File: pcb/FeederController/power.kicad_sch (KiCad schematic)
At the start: 20 parts, among them J17 12-24v DC, J18 5V Supply, Q1 DMP3028LK3-13, U4 AP2114-3.3, U5 AP63205WU

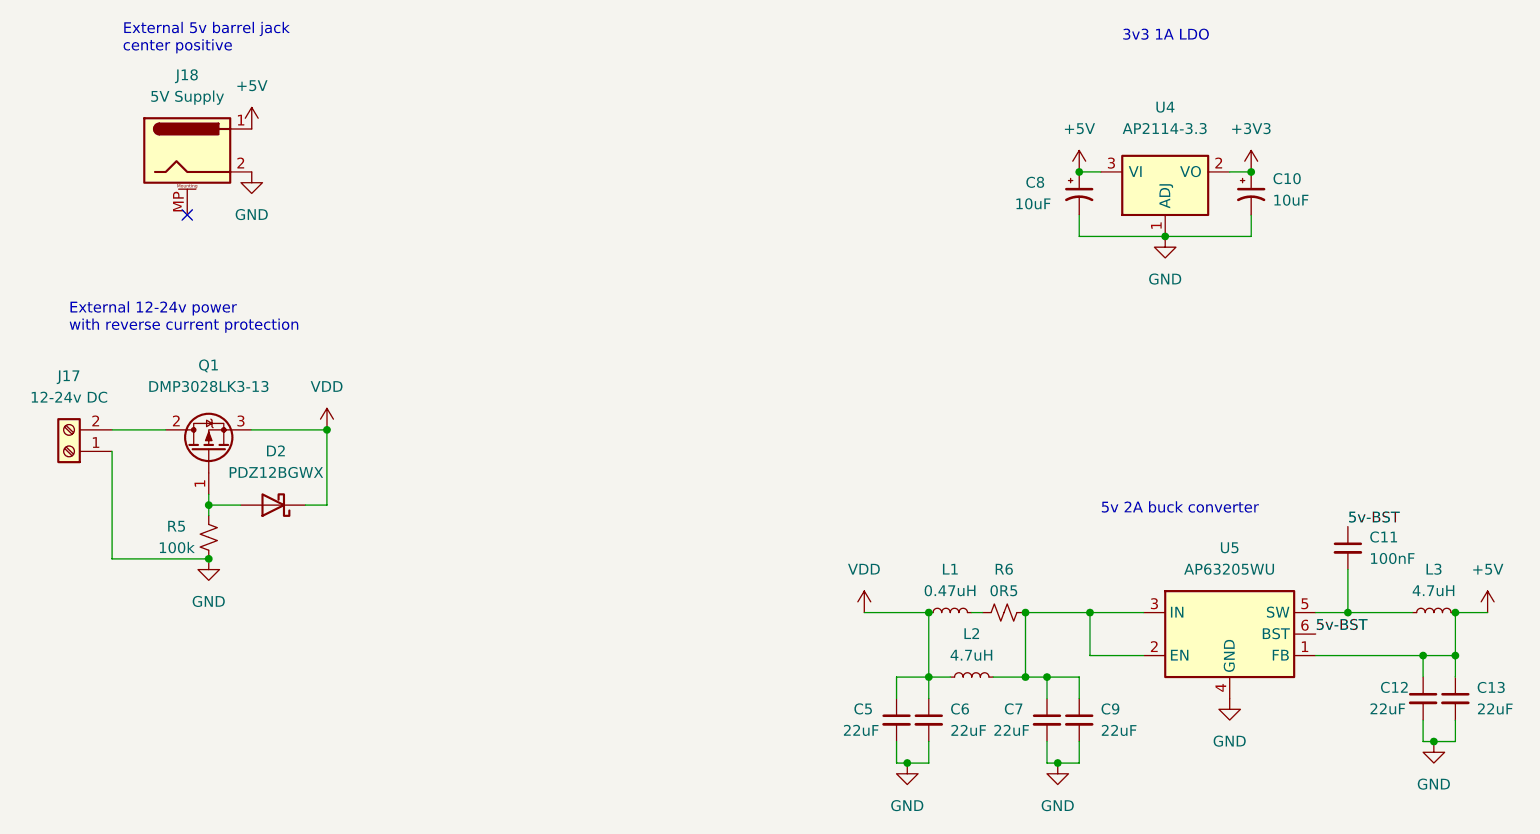
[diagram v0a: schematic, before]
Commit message: Update PCB as below
* Adjusted placement of mounting holes to line up with LumenPnP staging plate.
* Added 2k4 P/U for SDA/SCL.
* GND plane stitching
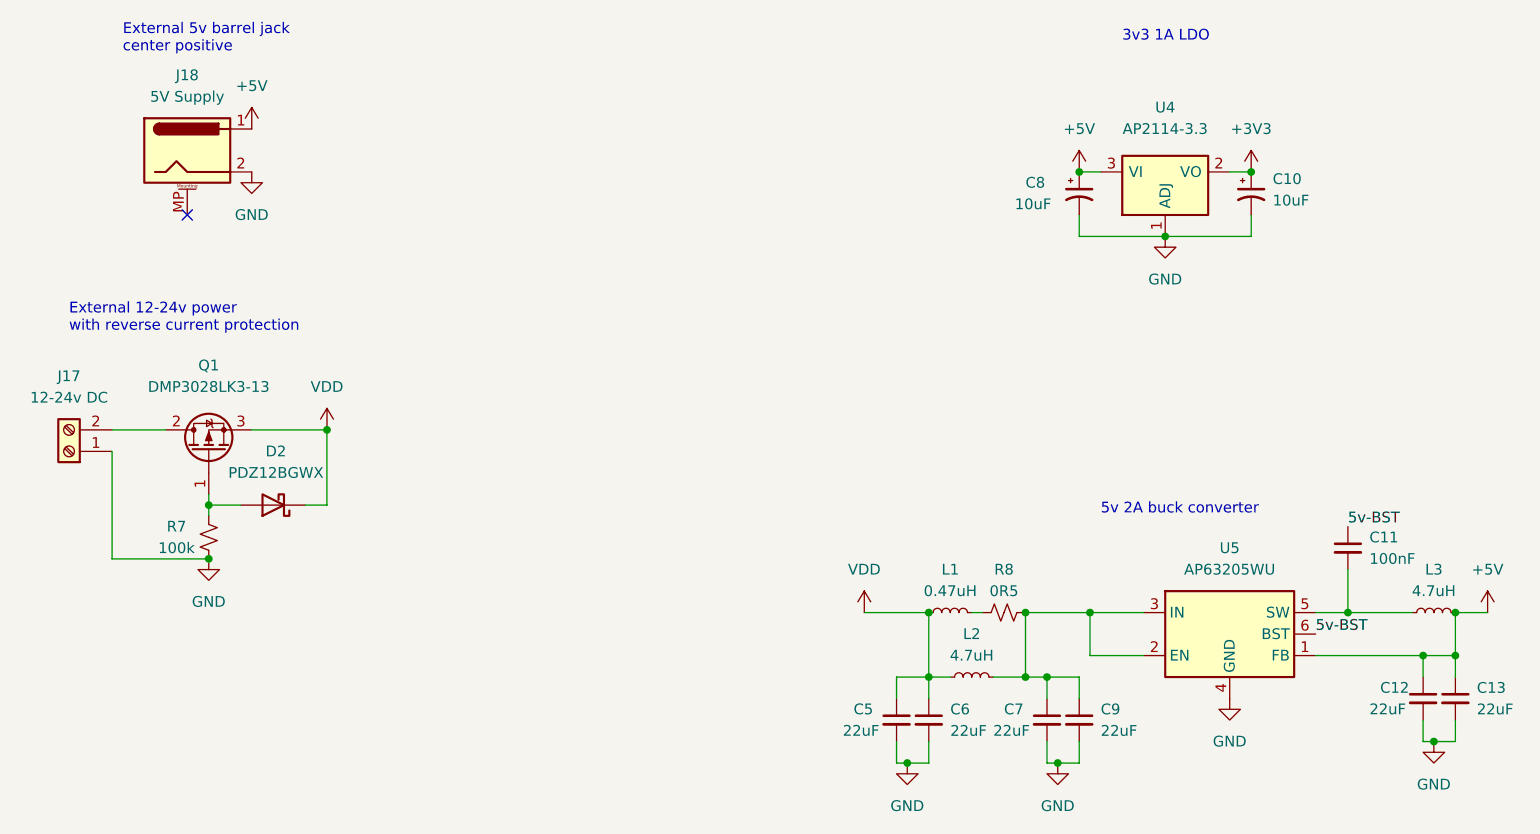
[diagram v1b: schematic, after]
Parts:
- renumbered R5 to R7, R6 to R8
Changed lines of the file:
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@@
   (symbol (lib_id "power:GND") (at 41.91 85.09 0) (unit 1)
     (in_bom yes) (on_board yes) (fields_autoplaced)
-    (property "Reference" "#PWR046" (id 0) (at 41.91 91.44 0)
+    (property "Reference" "#PWR047" (id 0) (at 41.91 91.44 0)
       (effects (font (size 1.27 1.27)) hide)
     )
@@
   (symbol (lib_id "power:+3V3") (at 165.1 39.37 0) (unit 1)
     (in_bom yes) (on_board yes) (fields_autoplaced)
-    (property "Reference" "#PWR056" (id 0) (at 165.1 43.18 0)
+    (property "Reference" "#PWR057" (id 0) (at 165.1 43.18 0)
       (effects (font (size 1.27 1.27)) hide)
     )
@@
   (symbol (lib_id "Device:R_Small_US") (at 135.89 91.44 90) (unit 1)
     (in_bom yes) (on_board yes)
-    (property "Reference" "R6" (id 0) (at 135.89 86.36 90))
+    (property "Reference" "R8" (id 0) (at 135.89 86.36 90))
     (property "Value" "0R5" (id 1) (at 135.89 88.9 90))
     (property "Footprint" "Resistor_SMD:R_0805_2012Metric_Pad1.20x1.40mm_HandSolder" (id 2) (at 135.89 91.44 0)
@@
   (symbol (lib_id "power:GND") (at 154.94 46.99 0) (unit 1)
     (in_bom yes) (on_board yes) (fields_autoplaced)
-    (property "Reference" "#PWR054" (id 0) (at 154.94 53.34 0)
+    (property "Reference" "#PWR055" (id 0) (at 154.94 53.34 0)
       (effects (font (size 1.27 1.27)) hide)
     )
@@
   (symbol (lib_id "power:+5V") (at 193.04 91.44 0) (unit 1)
     (in_bom yes) (on_board yes) (fields_autoplaced)
-    (property "Reference" "#PWR058" (id 0) (at 193.04 95.25 0)
+    (property "Reference" "#PWR059" (id 0) (at 193.04 95.25 0)
       (effects (font (size 1.27 1.27)) hide)
     )
@@
   (symbol (lib_id "power:+5V") (at 46.99 34.29 0) (unit 1)
     (in_bom yes) (on_board yes) (fields_autoplaced)
-    (property "Reference" "#PWR047" (id 0) (at 46.99 38.1 0)
+    (property "Reference" "#PWR048" (id 0) (at 46.99 38.1 0)
       (effects (font (size 1.27 1.27)) hide)
     )
@@
   (symbol (lib_id "power:GND") (at 186.69 106.68 0) (unit 1)
     (in_bom yes) (on_board yes) (fields_autoplaced)
-    (property "Reference" "#PWR057" (id 0) (at 186.69 113.03 0)
+    (property "Reference" "#PWR058" (id 0) (at 186.69 113.03 0)
       (effects (font (size 1.27 1.27)) hide)
     )
@@
   (symbol (lib_id "power:VDD") (at 55.88 69.85 0) (unit 1)
     (in_bom yes) (on_board yes) (fields_autoplaced)
-    (property "Reference" "#PWR049" (id 0) (at 55.88 73.66 0)
+    (property "Reference" "#PWR050" (id 0) (at 55.88 73.66 0)
       (effects (font (size 1.27 1.27)) hide)
     )
@@
   (symbol (lib_id "power:VDD") (at 119.38 91.44 0) (unit 1)
     (in_bom yes) (on_board yes) (fields_autoplaced)
-    (property "Reference" "#PWR050" (id 0) (at 119.38 95.25 0)
+    (property "Reference" "#PWR051" (id 0) (at 119.38 95.25 0)
       (effects (font (size 1.27 1.27)) hide)
     )
@@
   (symbol (lib_id "Device:R_Small_US") (at 41.91 82.55 180) (unit 1)
     (in_bom yes) (on_board yes)
-    (property "Reference" "R5" (id 0) (at 38.1 81.28 0))
+    (property "Reference" "R7" (id 0) (at 38.1 81.28 0))
     (property "Value" "100k" (id 1) (at 38.1 83.82 0))
     (property "Footprint" "Resistor_SMD:R_1206_3216Metric_Pad1.30x1.75mm_HandSolder" (id 2) (at 41.91 82.55 0)
@@
   (symbol (lib_id "power:GND") (at 142.24 109.22 0) (unit 1)
     (in_bom yes) (on_board yes) (fields_autoplaced)
-    (property "Reference" "#PWR052" (id 0) (at 142.24 115.57 0)
+    (property "Reference" "#PWR053" (id 0) (at 142.24 115.57 0)
       (effects (font (size 1.27 1.27)) hide)
     )
@@
   (symbol (lib_id "power:+5V") (at 144.78 39.37 0) (unit 1)
     (in_bom yes) (on_board yes) (fields_autoplaced)
-    (property "Reference" "#PWR053" (id 0) (at 144.78 43.18 0)
+    (property "Reference" "#PWR054" (id 0) (at 144.78 43.18 0)
       (effects (font (size 1.27 1.27)) hide)
     )
@@
   (symbol (lib_id "power:GND") (at 124.46 109.22 0) (unit 1)
     (in_bom yes) (on_board yes) (fields_autoplaced)
-    (property "Reference" "#PWR051" (id 0) (at 124.46 115.57 0)
+    (property "Reference" "#PWR052" (id 0) (at 124.46 115.57 0)
       (effects (font (size 1.27 1.27)) hide)
     )
@@
   (symbol (lib_id "power:GND") (at 162.56 101.6 0) (unit 1)
     (in_bom yes) (on_board yes) (fields_autoplaced)
-    (property "Reference" "#PWR055" (id 0) (at 162.56 107.95 0)
+    (property "Reference" "#PWR056" (id 0) (at 162.56 107.95 0)
       (effects (font (size 1.27 1.27)) hide)
     )
@@
   (symbol (lib_id "power:GND") (at 46.99 39.37 0) (unit 1)
     (in_bom yes) (on_board yes) (fields_autoplaced)
-    (property "Reference" "#PWR048" (id 0) (at 46.99 45.72 0)
-      (effects (font (size 1.27 1.27)) hide)
-    )
+    (property "Reference" "#PWR049" (id 0) (at 46.99 45.72 0)
+      (effects (font (size 1.27 1.27)) hide)
+    )
